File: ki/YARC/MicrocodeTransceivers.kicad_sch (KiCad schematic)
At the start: 5 parts, among them U66 74HC245, U67 74LS574, U68 74LS574, U69 74HC245, U70 74HC245

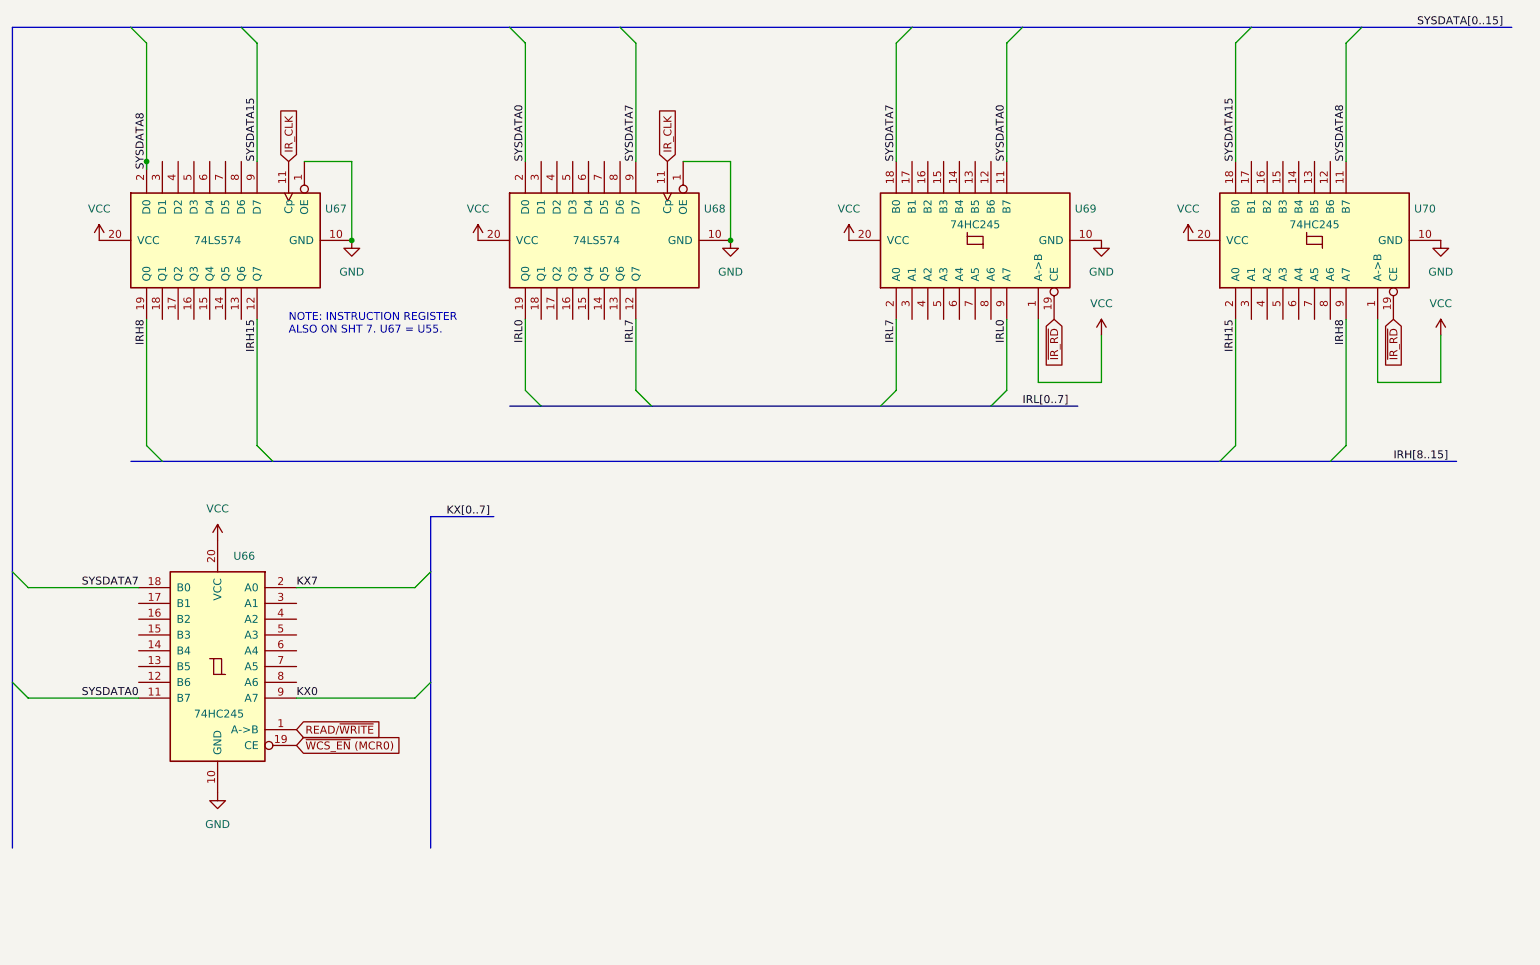
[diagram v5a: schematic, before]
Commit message: Add the ACN mini-bus which can come from the instruction bits 11:8 or from the microcode bits 23:20. It selects the ALU operation and the condition codes.
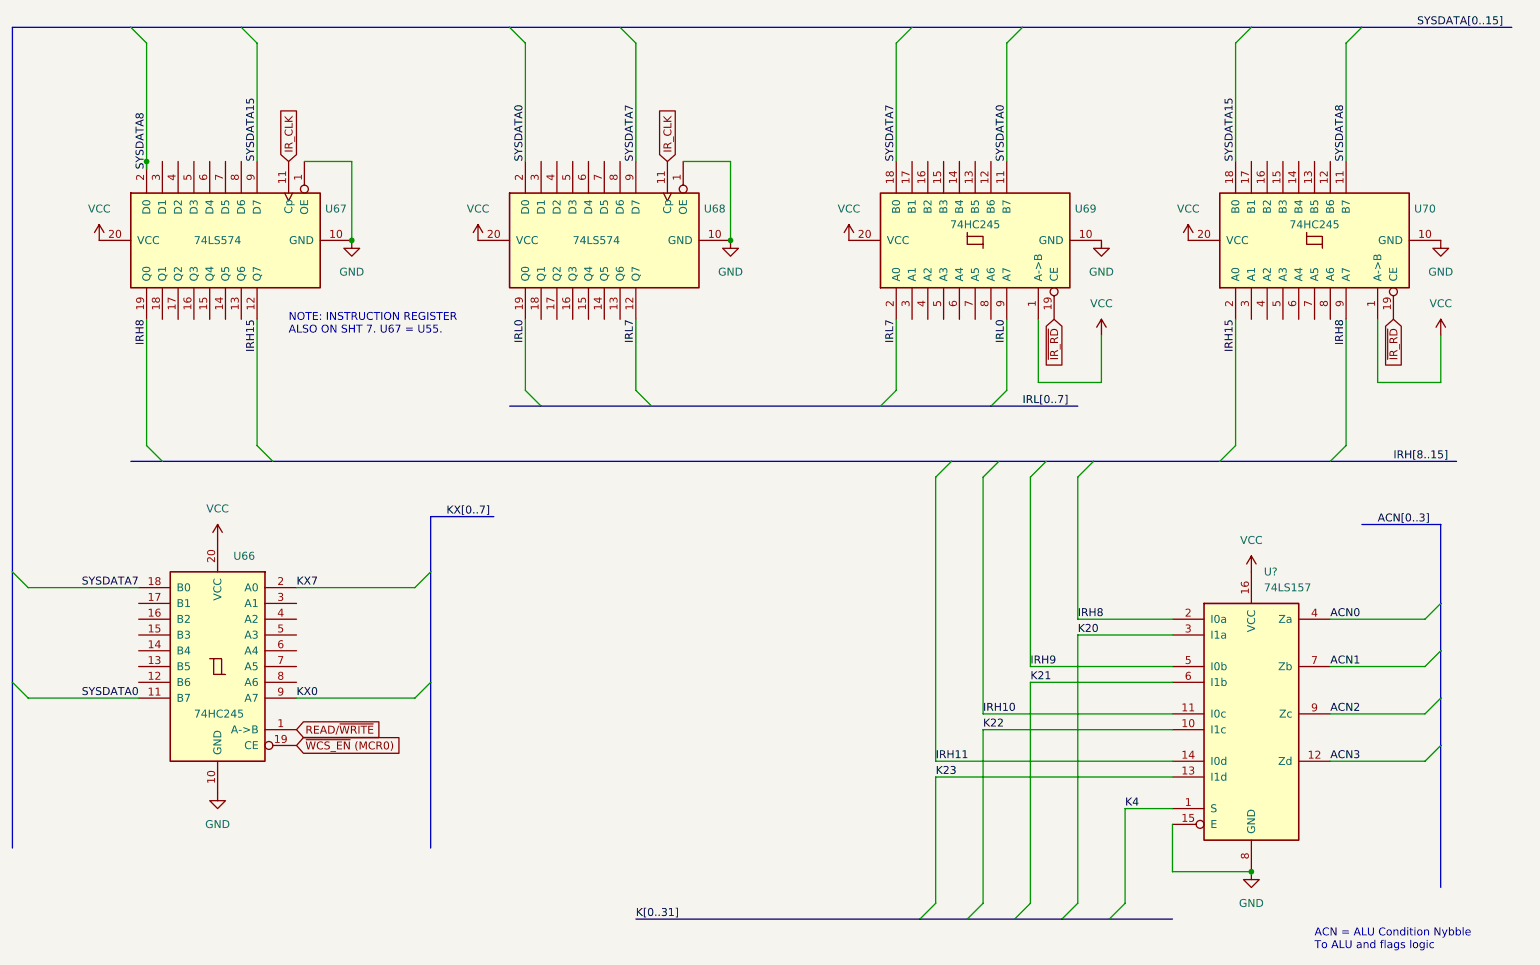
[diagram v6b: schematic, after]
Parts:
- added U?: 74LS157, symbol 74xx:74LS157
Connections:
- net GND: now also U?.15 (E), U?.8 (GND)
- net IRH8: now also U?.2 (I0a)
- net VCC: now also U?.16 (VCC)
- new net ACN0: U?.4 (Za)
- new net ACN1: U?.7 (Zb)
- new net ACN2: U?.9 (Zc)
- new net ACN3: U?.12 (Zd)
- new net IRH10: U?.11 (I0c)
- new net IRH11: U?.14 (I0d)
- new net IRH9: U?.5 (I0b)
- new net K20: U?.3 (I1a)
- new net K21: U?.6 (I1b)
- new net K22: U?.10 (I1c)
- new net K23: U?.13 (I1d)
- new net K4: U?.1 (S)
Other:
- note added: "ACN = ALU Condition Nybble To ALU and flags logic"

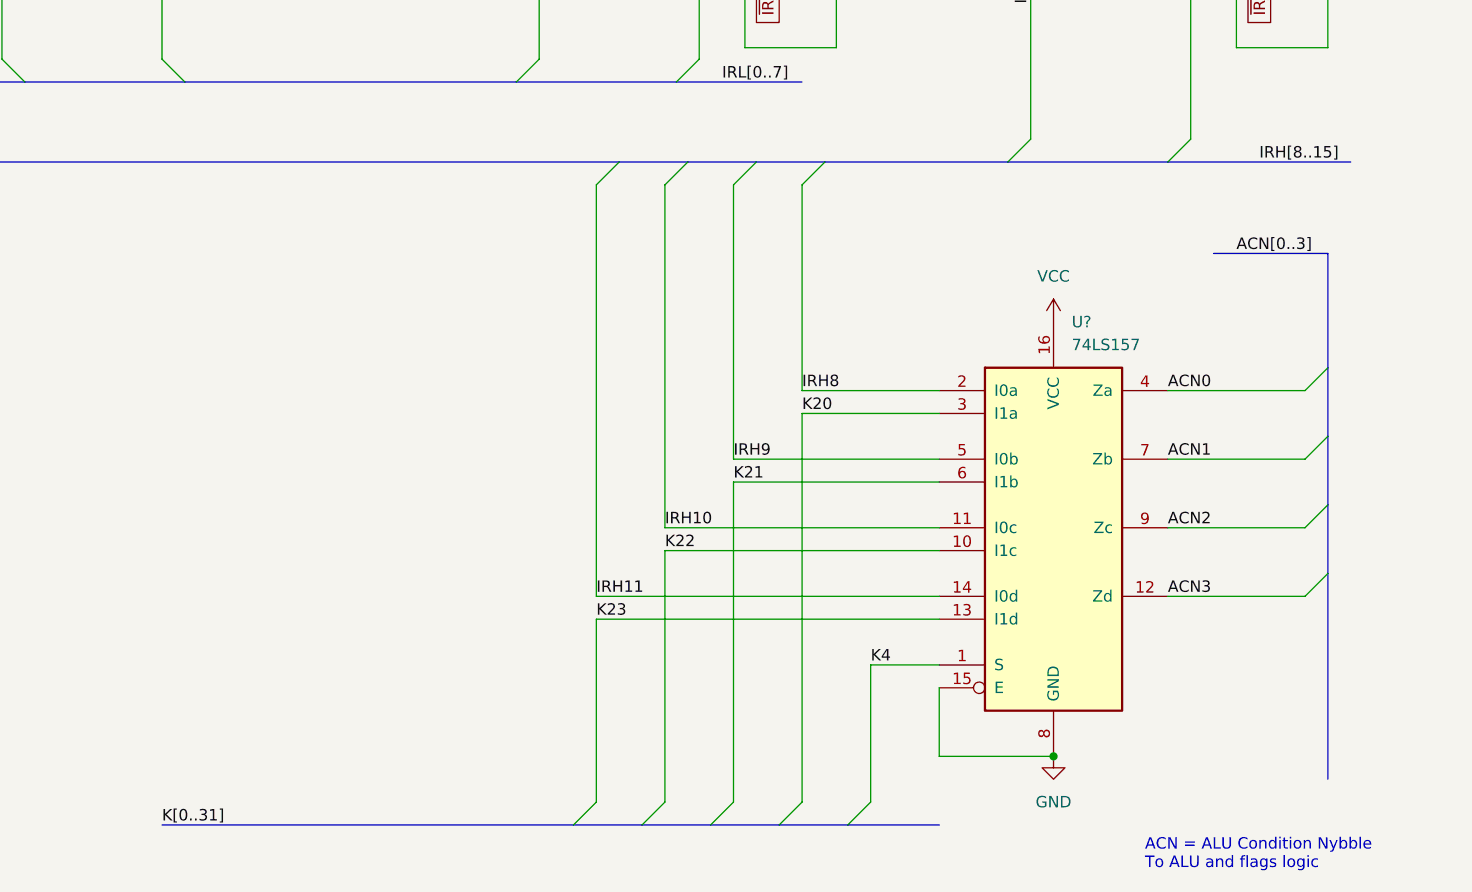
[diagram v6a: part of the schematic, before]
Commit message: Discovered that ACN mux was already drawn on another sheet of the schematic - fixed. Added ACN control bit to microcode. Ongoing cleanup: replaced acronym RSW with RCW in assembly language.
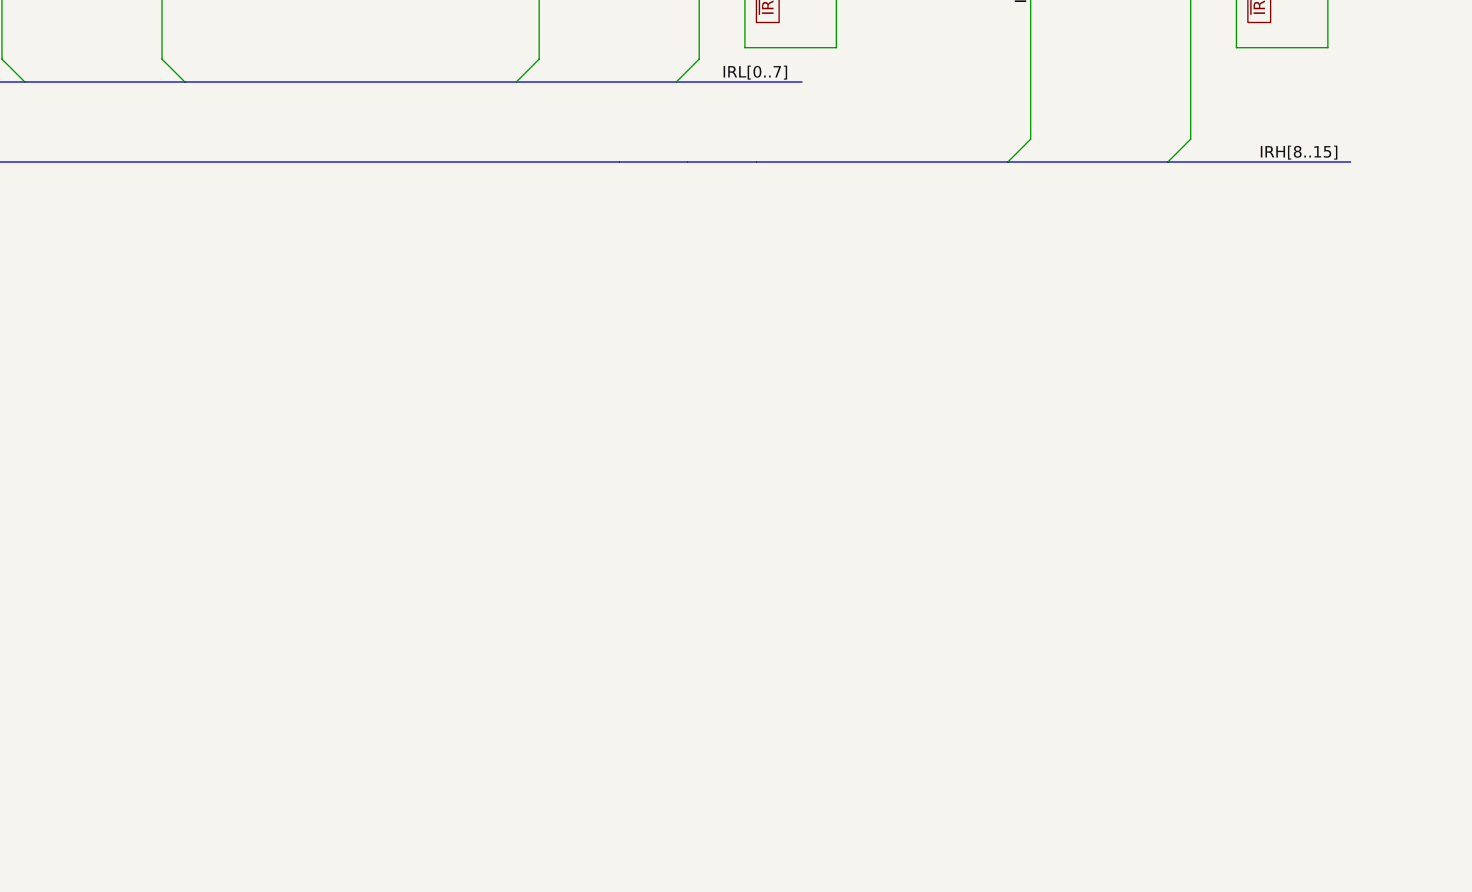
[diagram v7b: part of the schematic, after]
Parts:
- removed U?: 74LS157, symbol 74xx:74LS157
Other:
- note removed: "ACN = ALU Condition Nybble To ALU and flags logic"

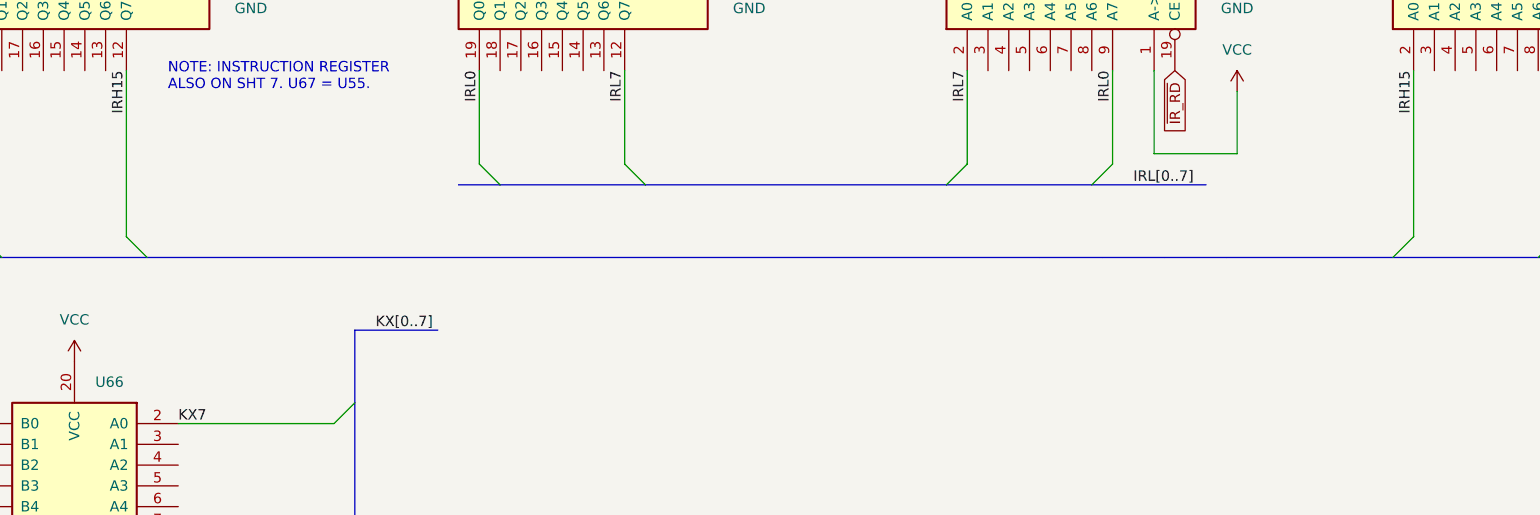
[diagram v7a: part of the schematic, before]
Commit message: Fix schematic error in <= gate. Cleanup signal naming. Fix subtle issue with carry in signal.
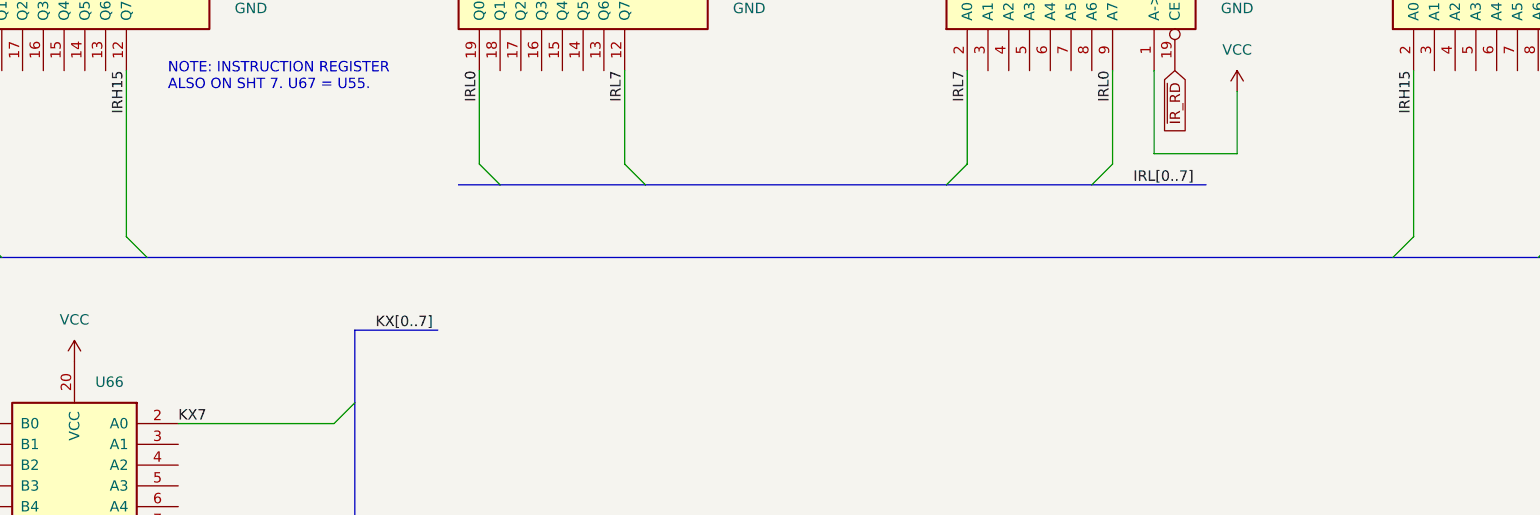
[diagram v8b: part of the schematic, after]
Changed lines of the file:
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@@
     (stroke (width 0) (type default) (color 0 0 0 0))
   )
-  (bus (pts (xy 177.8 88.9) (xy 185.42 88.9))
+  (bus (pts (xy 60.96 88.9) (xy 213.36 88.9))
     (stroke (width 0) (type default) (color 0 0 0 0))
   )
@@
     (stroke (width 0) (type default) (color 0 0 0 0))
   )
-  (bus (pts (xy 193.04 88.9) (xy 213.36 88.9))
-    (stroke (width 0) (type default) (color 0 0 0 0))
-  )
   (bus (pts (xy 43.18 88.9) (xy 60.96 88.9))
     (stroke (width 0) (type default) (color 0 0 0 0))
@@
   )
   (wire (pts (xy 238.76 66.04) (xy 238.76 76.2))
-    (stroke (width 0) (type default) (color 0 0 0 0))
-  )
-  (bus (pts (xy 185.42 88.9) (xy 193.04 88.9))
     (stroke (width 0) (type default) (color 0 0 0 0))
   )
@@
     (stroke (width 0) (type default) (color 0 0 0 0))
   )
-  (bus (pts (xy 170.18 88.9) (xy 177.8 88.9))
-    (stroke (width 0) (type default) (color 0 0 0 0))
-  )
-  (bus (pts (xy 60.96 88.9) (xy 170.18 88.9))
-    (stroke (width 0) (type default) (color 0 0 0 0))
-  )
